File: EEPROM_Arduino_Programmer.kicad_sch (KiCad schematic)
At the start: 4 parts, among them U1 74HC595

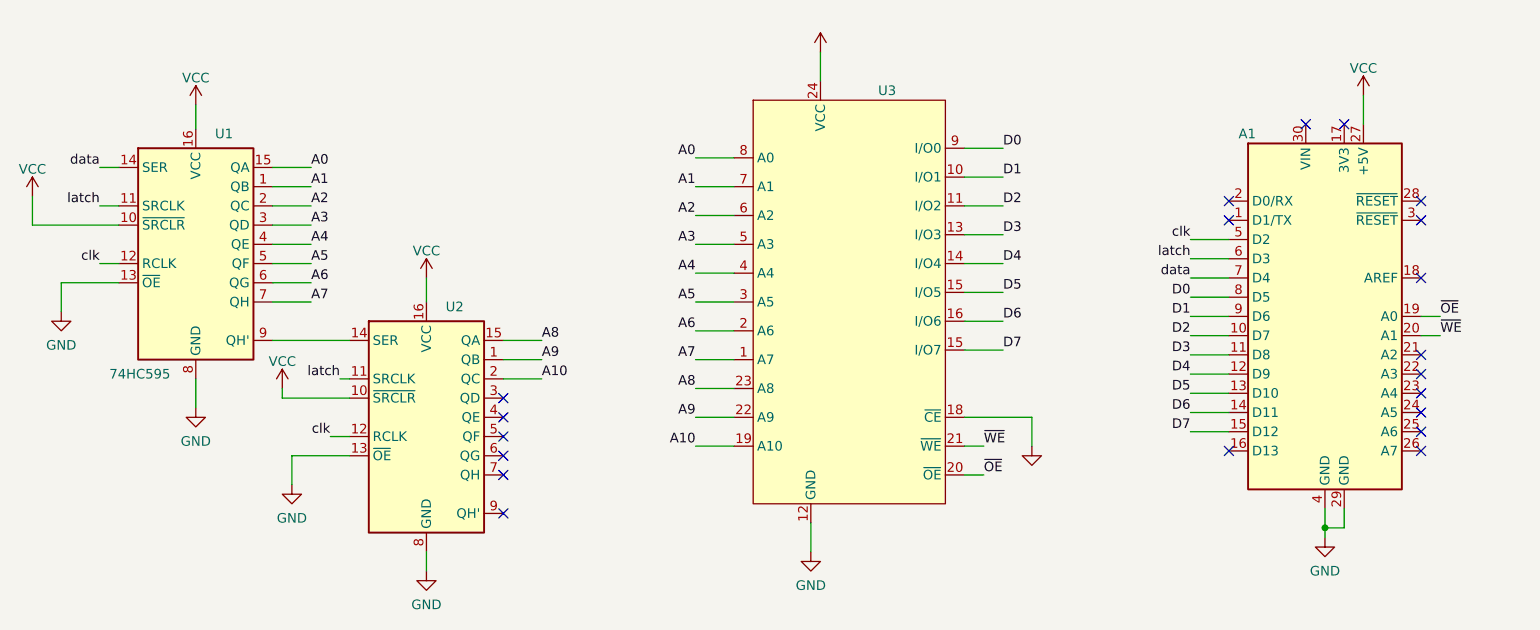
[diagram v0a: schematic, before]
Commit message: updated kicad version from 7 to 9!
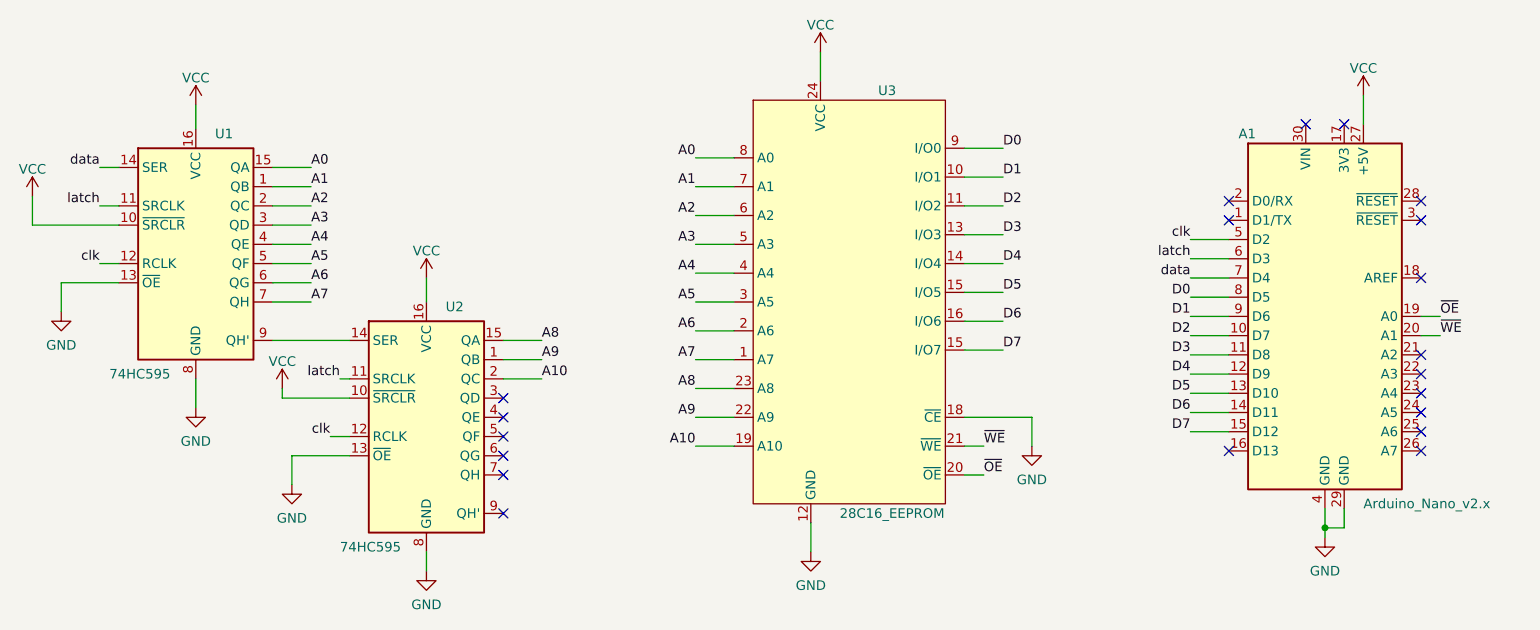
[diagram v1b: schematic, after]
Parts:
- A1: value (none) -> Arduino_Nano_v2.x; footprint (none) -> Module:Arduino_Nano
- U1: footprint (none) -> Package_DIP:DIP-16_W7.62mm
- U2: value (none) -> 74HC595; footprint (none) -> Package_DIP:DIP-16_W7.62mm
- U3: value (none) -> 28C16_EEPROM; footprint (none) -> Package_DIP:DIP-24_W15.24mm_Socket
